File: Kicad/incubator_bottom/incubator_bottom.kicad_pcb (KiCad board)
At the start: 2 copper layers, 100.1 x 73.7 mm, 59 parts, among them J1 Conn_01x02, J10 Conn_01x01, J11 Conn_01x01, J2 Conn_02x03_Odd_Even, J3 RJ12, J4 Conn_01x01, J5 AudioJack3_SwitchTR, J6 AudioJack3_SwitchTR, J7 Conn_01x02, J8 Conn_01x06, J9 Conn_01x01, Q1 ZXMS6004, Q2 IPB80N03S4L-03, U1 DS18B20Z, U2 DS18B20, U3 ATmega328P-AU, U4 ACT4088

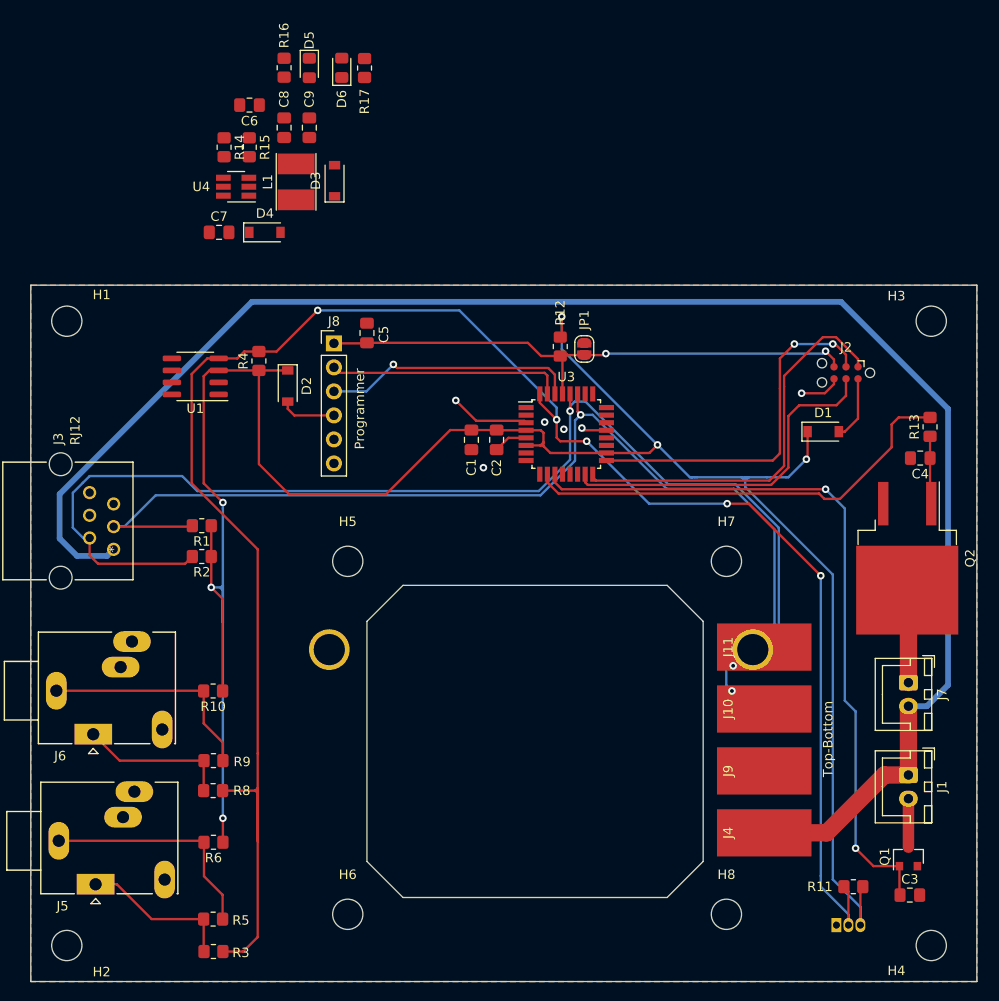
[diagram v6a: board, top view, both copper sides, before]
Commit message: fix: Routes and positions for Power resistor, 5V Step-down and uC were changed
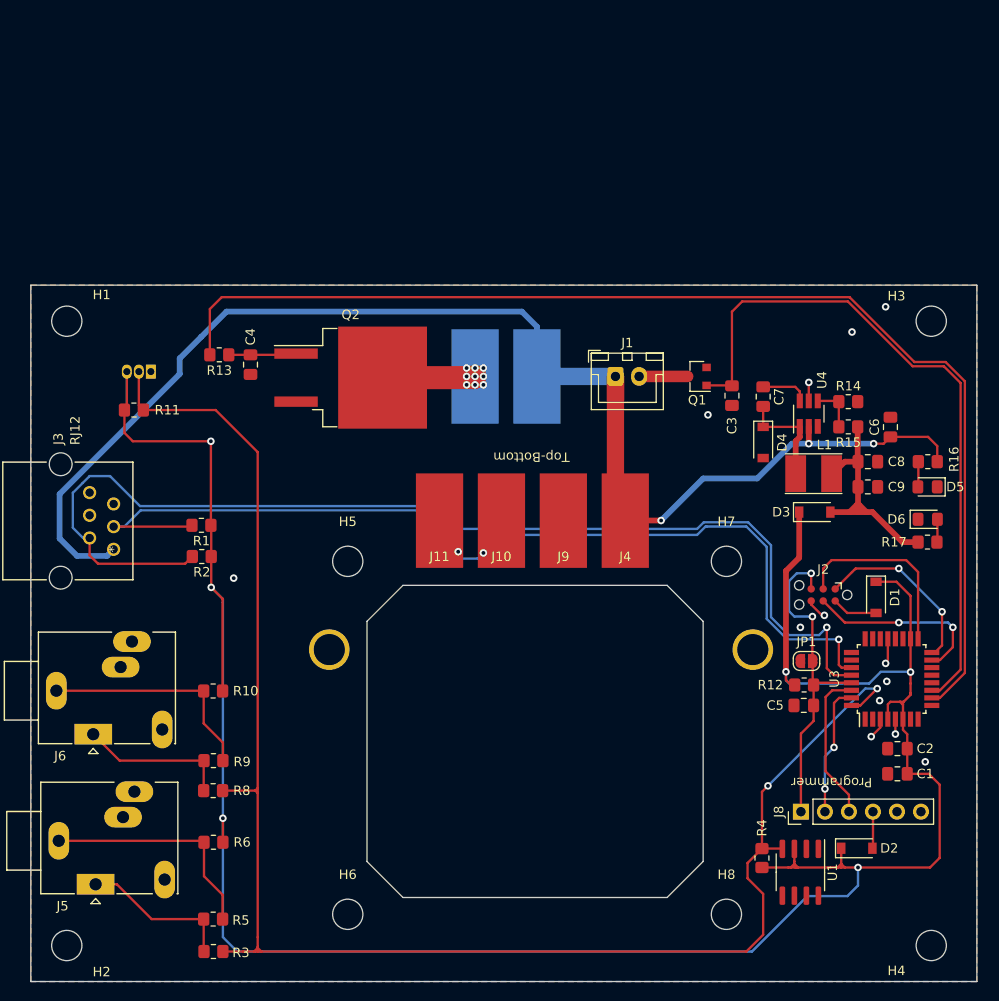
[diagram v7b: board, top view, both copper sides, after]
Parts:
- added J12: Conn_01x01, Connector_Wire:SolderWirePad_1x01_SMD_5x10mm, B.Cu at (115.1, 63.2)
- J7: value Conn_01x02 -> Conn_01x01; footprint Connector_JST:JST_XH_B2B-XH-A_1x02_P2.50mm_Vertical -> Connector_Wire:SolderWirePad_1x01_SMD_5x10mm; moved to B.Cu
- moved U2 93.2 mm to (80.8, 62.7), turned to 180 degrees
- moved R11 91.3 mm to (79.0, 66.8), turned to 0 degrees
- moved U1 82.8 mm to (149.5, 115.7), turned to 270 degrees
- moved R16 79.8 mm to (163.0, 72.3), turned to 180 degrees
- moved D5 79.0 mm to (162.9, 74.9), turned to 180 degrees
- moved D6 78.3 mm to (162.9, 78.4), turned to 0 degrees
- moved R17 77.9 mm to (162.9, 80.8), turned to 0 degrees
- moved D2 77.6 mm to (155.4, 113.2), turned to 0 degrees
- moved C6 75.9 mm to (159.0, 68.6), turned to 90 degrees
- moved R13 75.6 mm to (88.0, 61.0), turned to 180 degrees
- moved R4 74.8 mm to (145.4, 114.2)
- moved C4 71.5 mm to (91.3, 62.0), turned to 270 degrees
- moved R14 71.3 mm to (154.5, 65.9), turned to 180 degrees
- moved C8 71.1 mm to (156.6, 72.3), turned to 0 degrees
- moved C9 70.2 mm to (156.6, 74.9), turned to 0 degrees
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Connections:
- J7 pad 1: Net-(J7-Pad1) -> 12V
- Q2 pad 2: Net-(J7-Pad1) -> Net-(J12-Pad1)
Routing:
- net PID: track 47.0 -> 124.4 mm
- net 12V: track 178.0 -> 143.9 mm, vias 0 -> 3
- net ONE-WIRE: track 205.3 -> 173.0 mm, vias 5 -> 2
- net /5V Step-down/5V: track 0.00 -> 25.3 mm
- net ~RESET: track 58.9 -> 35.4 mm
- net MISO: track 42.2 -> 19.0 mm, vias 0 -> 2
- net SCK: track 38.1 -> 20.1 mm, vias 2 -> 0
- net MOSI: track 37.4 -> 19.8 mm, vias 0 -> 2
- net VIN: track 242.3 -> 258.8 mm
- net Net-(C7-Pad2): track 0.00 -> 11.2 mm
- net TX: track 24.9 -> 14.0 mm, vias 0 -> 2
- net RX: track 27.0 -> 16.2 mm, vias 1 -> 0
- net Net-(J12-Pad1): track 0.00 -> 10.0 mm, vias 0 -> 9
- net Net-(J7-Pad1): track 9.83 -> 0.00 mm
- net SDA: track 114.9 -> 105.9 mm
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
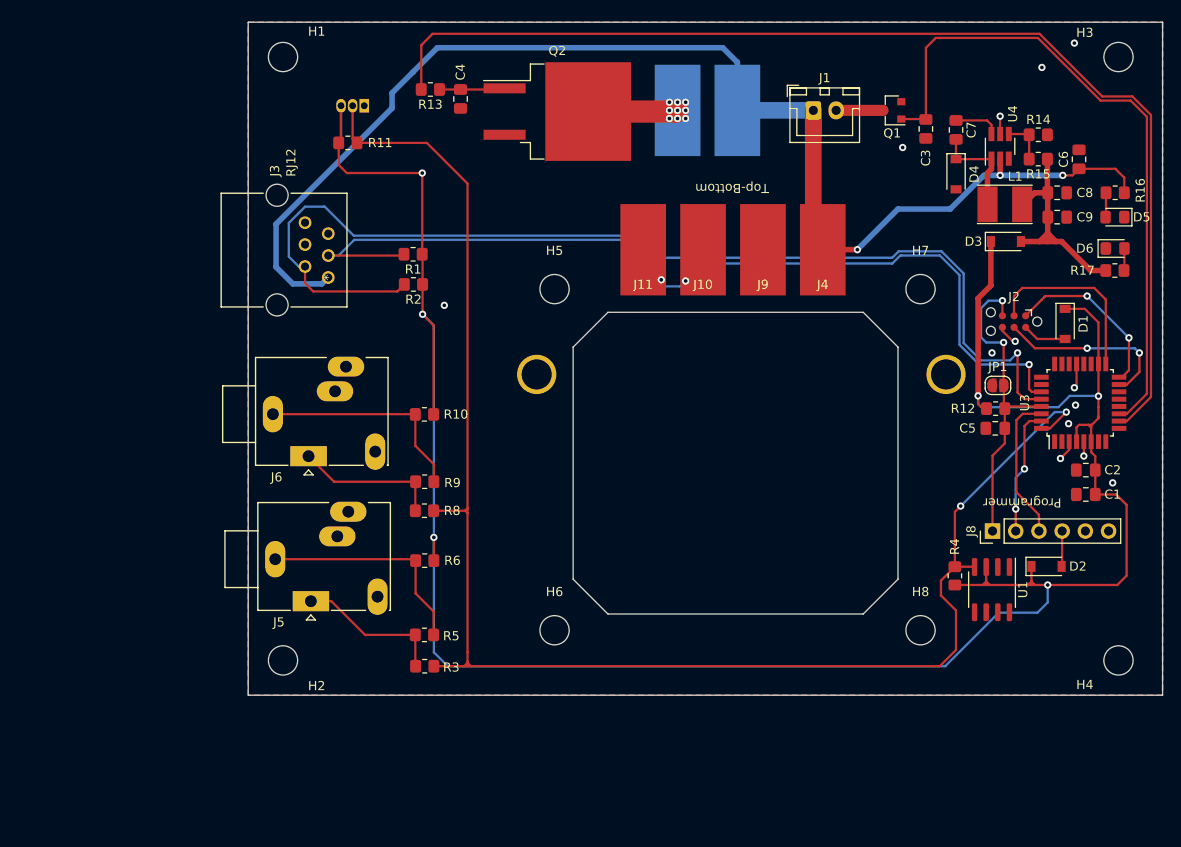
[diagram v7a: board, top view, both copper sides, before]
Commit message: refactor: Fan/resistor position, pad top-bottom
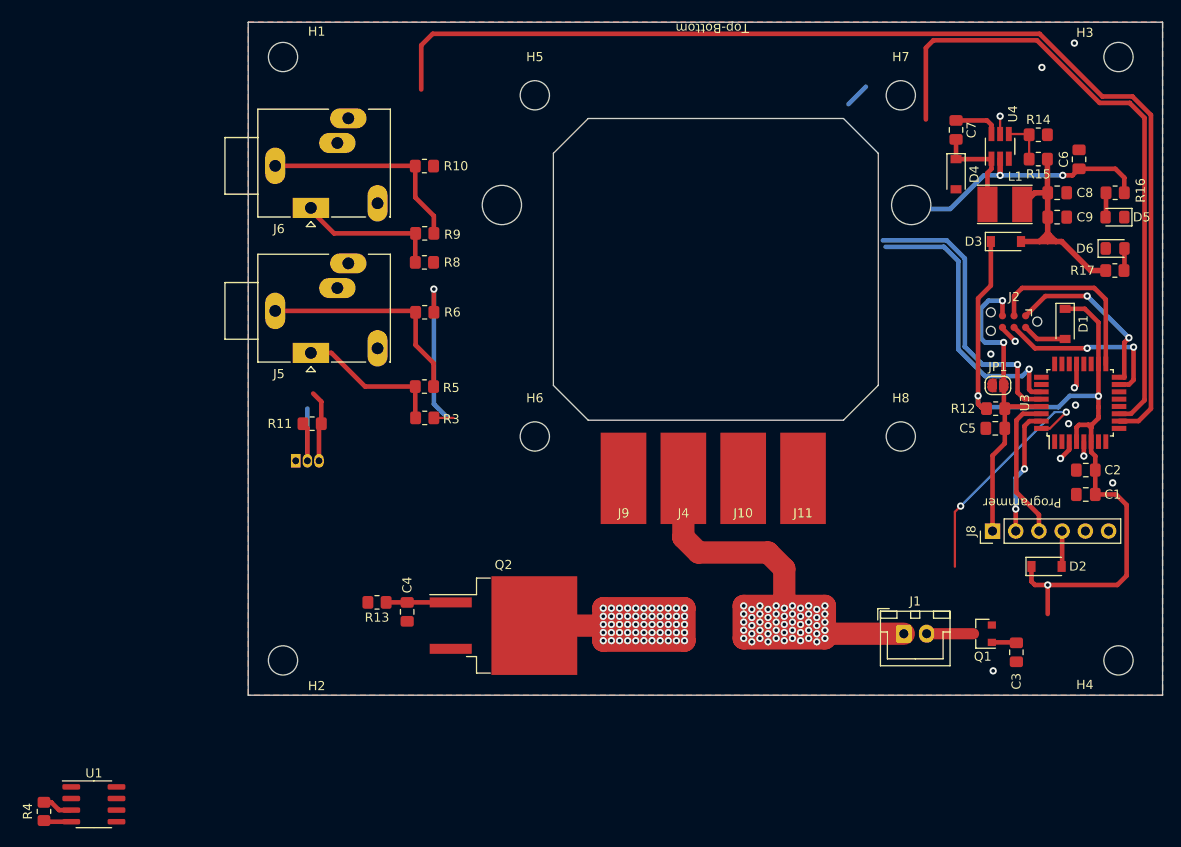
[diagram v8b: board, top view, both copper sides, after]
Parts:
- removed J3: RJ12, Incubator:E5566-Q0LK22-L
- removed R1, R2: 10k, Resistor_SMD:R_0805_2012Metric_Pad1.20x1.40mm_HandSolder
- moved R4 103.0 mm to (45.7, 140.0), turned to 270 degrees
- moved U1 101.1 mm to (51.2, 139.2), turned to 0 degrees
- moved J1 58.1 mm to (139.8, 120.5)
- moved Q1 58.1 mm to (148.5, 120.5)
- moved C3 58.1 mm to (152.1, 122.6)
- moved Q2 56.6 mm to (96.0, 119.6)
- moved J7 56.5 mm to (126.7, 119.5), turned to 90 degrees
- moved C4 56.4 mm to (85.5, 118.1)
- moved R13 56.4 mm to (82.2, 117.1)
- moved J12 56.4 mm to (111.4, 119.5), turned to 90 degrees
- moved U2 39.6 mm to (73.3, 101.6), turned to 0 degrees
- moved R11 31.0 mm to (75.1, 97.5), turned to 180 degrees
- moved J11 30.5 mm to (128.8, 103.5)
- moved J9 29.3 mm to (109.1, 103.5)
- moved J4 29.3 mm to (115.7, 103.5)
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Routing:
- net VIN: track 258.8 -> 117.5 mm, vias 6 -> 4
- net ONE-WIRE: track 173.0 -> 41.4 mm
- net SCL: track 123.9 -> 32.0 mm, vias 2 -> 1
- net SDA: track 105.9 -> 33.9 mm, vias 2 -> 1
- net Net-(J12-Pad1): track 10.0 -> 47.6 mm, vias 9 -> 55
- net 12V: track 143.9 -> 112.6 mm, vias 3 -> 57
- net PID: track 124.4 -> 126.0 mm
- net GND: track 11.0 -> 10.9 mm, vias 13 -> 12
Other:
- outline, holes or cut-outs redrawn
- net class Min added: clearance 0.2, trace_width 0.508, via_dia 1, via_drill 0.5
